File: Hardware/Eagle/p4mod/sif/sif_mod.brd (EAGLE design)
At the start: 19.8 x 10.8 mm, 29 parts

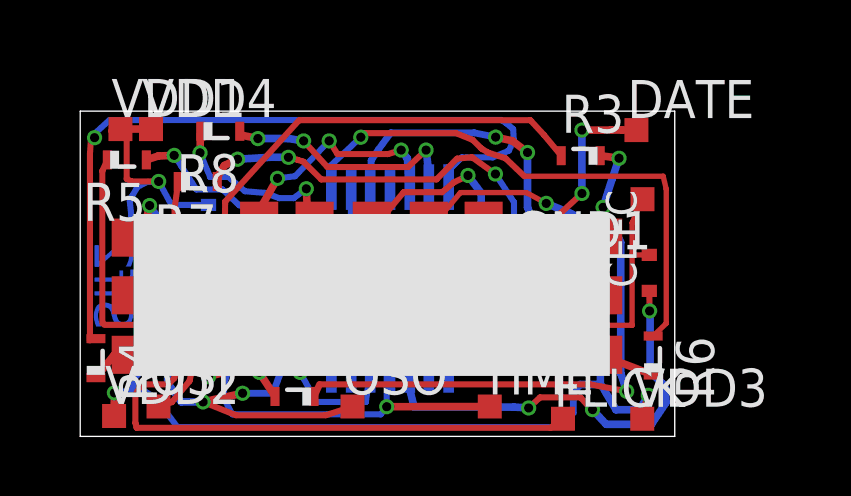
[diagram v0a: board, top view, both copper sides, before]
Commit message: Pushed VCAP to the bootm layer.
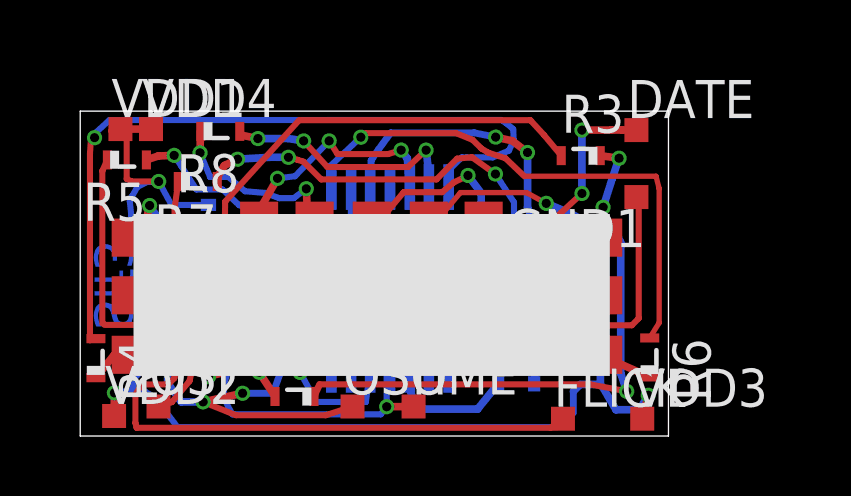
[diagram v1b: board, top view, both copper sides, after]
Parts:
- moved CEFC 5.77 mm to (15.7, 1.91), flipped to the bottom, turned to 180 degrees
- moved TIME 2.54 mm to (12.3, 1.15)
- moved GND1 0.21 mm to (19.8, 8.13)
- moved R6 0.13 mm to (20.2, 2.79)
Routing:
- net VDDCORE/VCAP: track 14.5 -> 4.46 mm, vias 3 -> 0
- net RA5/SW4: track 12.4 -> 9.81 mm
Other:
- board size 19.8 x 10.8 mm -> 19.6 x 10.8 mm
- board text added: "Sif3"
- board text removed: "Sif2"

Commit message: Optimizations.
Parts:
- moved VDD3 0.19 mm to (19.8, 0.75)
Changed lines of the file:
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@@
 <attribute name="TP_SIGNAL_NAME" value="" x="2.34269375" y="0.836640625" size="1.778" layer="27" display="off"/>
 </element>
-<element name="VDD3" library="testpad" package="TP08SQ" value="TPTP08SQ" x="19.94685625" y="0.745434375">
-<attribute name="TP_SIGNAL_NAME" value="" x="19.94685625" y="0.745434375" size="1.778" layer="27" display="off"/>
+<element name="VDD3" library="testpad" package="TP08SQ" value="TPTP08SQ" x="19.754278125" y="0.745434375">
+<attribute name="TP_SIGNAL_NAME" value="" x="19.754278125" y="0.745434375" size="1.778" layer="27" display="off"/>
 </element>
 <element name="VDD1" library="testpad" package="TP08SQ" value="TPTP08SQ" x="2.554646875" y="10.4011125">
@@
 <wire x1="18.6182" y1="1.8143125" x2="18.55316875" y2="1.88485625" width="0.1524" layer="16"/>
 <via x="20.148546875" y="1.526584375" extent="1-16" drill="0.3048"/>
-<wire x1="20.148546875" y1="1.526584375" x2="19.94685625" y2="0.745434375" width="0.254" layer="1"/>
+<wire x1="20.148546875" y1="1.526584375" x2="19.754278125" y2="0.745434375" width="0.254" layer="1"/>
 <wire x1="2.92190625" y1="8.65561875" x2="3.82825625" y2="8.65421875" width="0.2032" layer="1"/>
 <wire x1="3.82825625" y1="8.65421875" x2="4.256571875" y2="7.87175" width="0.2032" layer="16"/>

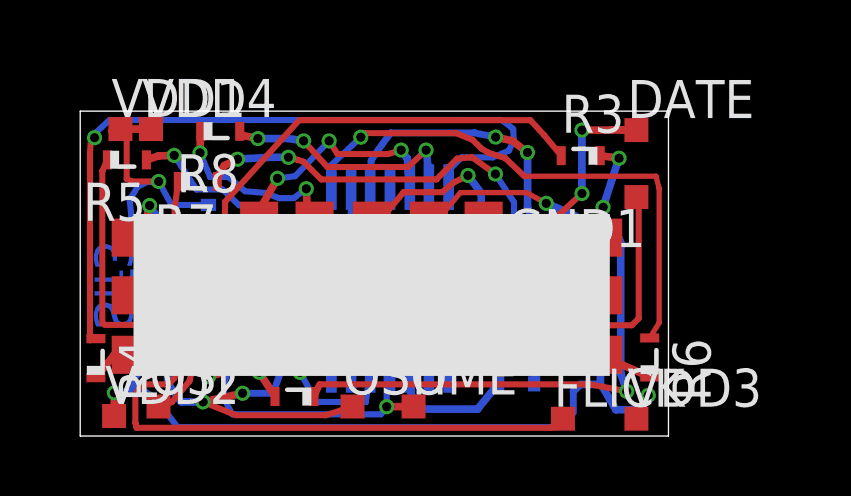
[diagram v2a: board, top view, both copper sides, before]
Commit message: Optimized SiF layout.
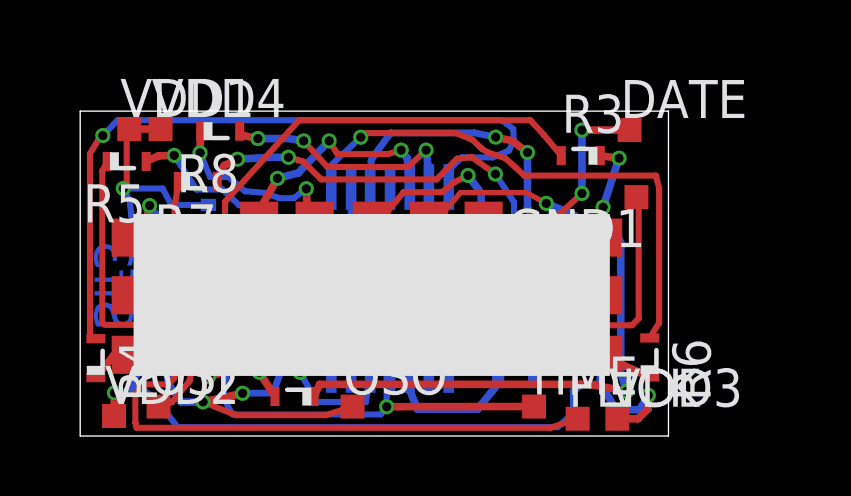
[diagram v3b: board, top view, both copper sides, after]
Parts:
- moved TIME 4.02 mm to (16.3, 1.15)
- moved VDD3 0.63 mm to (19.1, 0.75)
- moved FLICK 0.49 mm to (17.8, 0.75)
- moved VDD4 0.32 mm to (3.89, 10.4)
- moved VDD1 0.29 mm to (2.85, 10.4)
- moved DATE 0.23 mm to (19.5, 10.4)
- moved C4 0.12 mm to (4.12, 5.20)
- moved CEFC 0.11 mm to (15.7, 2.02)
- moved MCLR 0.06 mm to (16.7, 4.95)
- moved R5 0.05 mm to (2.76, 9.32)
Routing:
- net RA5/SW4: track 9.81 -> 13.8 mm

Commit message: Improved one trace to make it less likely to short it when soldering the board.
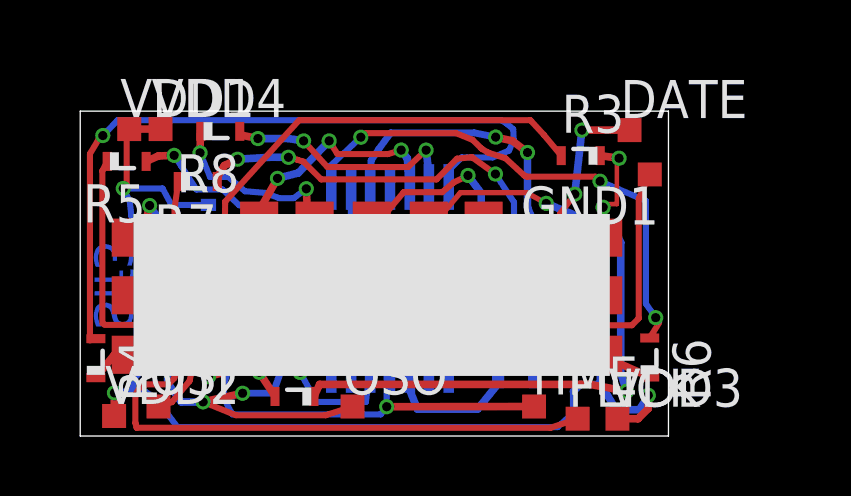
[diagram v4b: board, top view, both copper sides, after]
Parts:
- moved GND1 0.87 mm to (20.2, 8.89)
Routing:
- net RC7/LED_M5: track 18.0 -> 17.2 mm, vias 1 -> 3
- net GND: track 41.3 -> 42.1 mm
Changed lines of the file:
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@@
 <attribute name="TP_SIGNAL_NAME" value="" x="19.5248" y="10.36688125" size="1.778" layer="27" display="off"/>
 </element>
-<element name="GND1" library="testpad" package="TP08SQ" value="TPTP08SQ" x="19.753909375" y="8.1346" rot="R180">
-<attribute name="TP_SIGNAL_NAME" value="" x="19.753909375" y="8.1346" size="1.778" layer="27" rot="R180" display="off"/>
+<element name="GND1" library="testpad" package="TP08SQ" value="TPTP08SQ" x="20.199571875" y="8.8875125" rot="R180">
+<attribute name="TP_SIGNAL_NAME" value="" x="20.199571875" y="8.8875125" size="1.778" layer="27" rot="R180" display="off"/>
 </element>
 <element name="C1" library="resistor_mod" package="C0402K" value="12 pF" x="5.447440625" y="3.97883125" rot="MR0"/>
@@
 <wire x1="19.602871875" y1="3.86029375" x2="19.8312625" y2="4.093390625" width="0.2032" layer="1"/>
 <wire x1="19.8312625" y1="4.093390625" x2="19.8312625" y2="8.078559375" width="0.2032" layer="1"/>
-<wire x1="19.8312625" y1="8.078559375" x2="19.753909375" y2="8.1346" width="0.1524" layer="1"/>
+<wire x1="19.8312625" y1="8.078559375" x2="20.199571875" y2="8.8875125" width="0.2032" layer="1"/>
 </signal>
 <signal name="MCLR">
@@
 <wire x1="14.80681875" y1="9.617128125" x2="15.390496875" y2="9.427090625" width="0.2032" layer="1"/>
 <wire x1="15.390496875" y1="9.427090625" x2="16.0167375" y2="8.849990625" width="0.2032" layer="1"/>
-<wire x1="20.406696875" y1="8.849990625" x2="16.0167375" y2="8.849990625" width="0.2032" layer="1"/>
 <wire x1="20.19658125" y1="3.43789375" x2="20.511884375" y2="3.943603125" width="0.2032" layer="1"/>
-<wire x1="20.511884375" y1="3.943603125" x2="20.511884375" y2="8.4177625" width="0.2032" layer="1"/>
-<wire x1="20.511884375" y1="8.4177625" x2="20.406696875" y2="8.849990625" width="0.2032" layer="1"/>
+<wire x1="20.3962" y1="4.1148" x2="20.4724" y2="4.0386" width="0.1524" layer="1"/>
+<wire x1="20.07073125" y1="4.580390625" x2="20.3962" y2="4.1148" width="0.2032" layer="16"/>
+<wire x1="18.3896" y1="8.8138" x2="18.542" y2="8.6614" width="0.2032" layer="1"/>
+<wire x1="16.1036" y1="8.8138" x2="18.3896" y2="8.8138" width="0.2032" layer="1"/>
+<wire x1="20.4724" y1="4.0386" x2="20.511884375" y2="3.943603125" width="0.1524" layer="1"/>
+<wire x1="16.1036" y1="8.8138" x2="16.0167375" y2="8.849990625" width="0.2032" layer="1"/>
+<via x="20.3962" y="4.1148" extent="1-16" drill="0.3048"/>
+<via x="18.542" y="8.6614" extent="1-16" drill="0.3048"/>
+<wire x1="20.07073125" y1="4.580390625" x2="20.07073125" y2="8.009390625" width="0.2032" layer="16"/>
+<wire x1="20.07073125" y1="8.009390625" x2="18.542" y2="8.6614" width="0.2032" layer="16"/>
 </signal>
 <signal name="RB5/LED_H1">
@@
 <contactref element="R16" pad="1"/>
 <contactref element="DATE" pad="TP"/>
-<wire x1="17.937059375" y1="8.25389375" x2="17.937059375" y2="10.367015625" width="0.254" layer="16"/>
-<wire x1="17.21825625" y1="7.5912875" x2="17.937059375" y2="8.25389375" width="0.2032" layer="1"/>
+<wire x1="17.69888125" y1="8.231965625" x2="17.937059375" y2="10.367015625" width="0.254" layer="16"/>
+<wire x1="17.21825625" y1="7.5912875" x2="17.69888125" y2="8.231965625" width="0.2032" layer="1"/>
 <wire x1="16.57660625" y1="5.898040625" x2="17.21825625" y2="7.5912875" width="0.2032" layer="1"/>
 <wire x1="16.70376875" y1="6.269590625" x2="16.57660625" y2="5.898040625" width="0.2032" layer="16"/>
@@
 <wire x1="15.97174375" y1="3.4636125" x2="16.071203125" y2="3.62945" width="0.254" layer="16"/>
 <via x="17.937059375" y="10.367015625" extent="1-16" drill="0.3048"/>
-<via x="17.937059375" y="8.25389375" extent="1-16" drill="0.3048"/>
+<via x="17.69888125" y="8.231965625" extent="1-16" drill="0.3048"/>
 <via x="16.57660625" y="5.898040625" extent="1-16" drill="0.3048"/>
 <wire x1="17.905321875" y1="6.0561125" x2="17.905321875" y2="5.020053125" width="0.2032" layer="16"/>
@@
 <via x="18.6436" y="7.79409375" extent="1-16" drill="0.3048"/>
 <wire x1="18.5472875" y1="9.51516875" x2="19.17488125" y2="9.428203125" width="0.254" layer="1"/>
-<wire x1="18.6436" y1="7.79409375" x2="18.949809375" y2="8.75723125" width="0.254" layer="16"/>
-<wire x1="18.949809375" y1="8.75723125" x2="19.17488125" y2="9.428203125" width="0.254" layer="16"/>
+<wire x1="19.1008" y1="7.8994" x2="19.1008" y2="9.3218" width="0.1524" layer="1"/>
+<wire x1="18.6944" y1="7.8994" x2="19.1008" y2="7.8994" width="0.1524" layer="1"/>
+<wire x1="19.1008" y1="9.3218" x2="19.17488125" y2="9.428203125" width="0.1524" layer="1"/>
+<wire x1="18.6944" y1="7.8994" x2="18.6436" y2="7.79409375" width="0.1524" layer="1"/>
 </signal>
 <signal name="N$10">

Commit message: Reworked PCB edges for the Sif module.
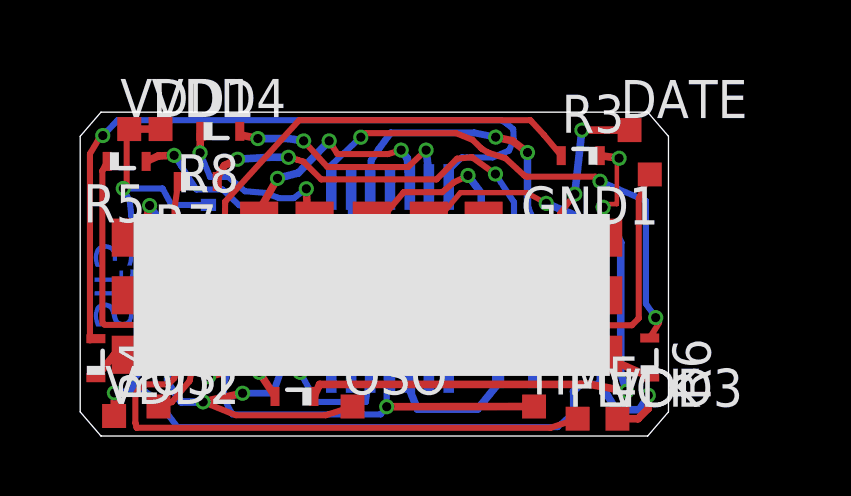
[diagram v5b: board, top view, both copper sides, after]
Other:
- outline, holes or cut-outs redrawn
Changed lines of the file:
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@@
 <board>
 <plain>
-<wire x1="1.213590625" y1="0.169440625" x2="1.213590625" y2="10.998596875" width="0" layer="20"/>
-<wire x1="1.213590625" y1="10.998596875" x2="20.822028125" y2="10.998596875" width="0" layer="20"/>
-<wire x1="20.822028125" y1="10.998596875" x2="20.822028125" y2="0.169440625" width="0" layer="20"/>
-<wire x1="20.822028125" y1="0.169440625" x2="1.213590625" y2="0.169440625" width="0" layer="20"/>
+<wire x1="20.822028125" y1="10.16" x2="20.822028125" y2="0.97388125" width="0" layer="20"/>
 <text x="2.96085" y="6.690371875" size="1.27" layer="16" font="vector" ratio="15" rot="MR270">Sif3</text>
+<wire x1="20.13061875" y1="10.964440625" x2="1.905" y2="10.964440625" width="0" layer="20"/>
+<wire x1="1.213590625" y1="0.97388125" x2="1.213590625" y2="10.16" width="0" layer="20"/>
+<wire x1="1.213590625" y1="10.16" x2="1.905" y2="10.964440625" width="0" layer="20"/>
+<wire x1="20.13061875" y1="10.964440625" x2="20.822028125" y2="10.16" width="0" layer="20"/>
+<wire x1="20.13054375" y1="0.169440625" x2="1.905" y2="0.169440625" width="0" layer="20"/>
+<wire x1="1.213590625" y1="0.97388125" x2="1.905" y2="0.169440625" width="0" layer="20"/>
+<wire x1="20.13054375" y1="0.169440625" x2="20.822028125" y2="0.97388125" width="0" layer="20"/>
 </plain>
 <attributes>
